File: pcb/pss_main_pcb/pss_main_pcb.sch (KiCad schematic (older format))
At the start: 29 parts

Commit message: Fix schematics
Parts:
- removed C?: C, symbol Device:C
- removed R?: R, symbol Device:R
- added R?: 1k, symbol Device:R
- C? (x2): value 680uF/50V -> 470uF/50V
- C?: value 220uF/16V -> 270uF/10V
- C?: value 220uF/16V -> 330uF/10V
- L?: value 33uH -> 68uH
- L?: value 33uH -> 47uH
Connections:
- net +3V3: now also R?.1
- net GND: no longer U?.5 (~ON~/OFF)
- new net Enable_5V: R?.2, U?.5 (~ON~/OFF)
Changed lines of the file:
@@
 Wire Wire Line
 	9950 1500 9950 1650
-$Comp
-L Device:R R?
-U 1 1 5E946DFD
-P 10350 1700
-F 0 "R?" H 10420 1746 50  0000 L CNN
-F 1 "R" H 10420 1655 50  0000 L CNN
-F 2 "" V 10280 1700 50  0001 C CNN
-F 3 "~" H 10350 1700 50  0001 C CNN
-	1    10350 1700
-	1    0    0    -1
-$EndComp
-$Comp
-L Device:C C?
-U 1 1 5E946EC3
-P 10350 2050
-F 0 "C?" H 10465 2096 50  0000 L CNN
-F 1 "C" H 10465 2005 50  0000 L CNN
-F 2 "" H 10388 1900 50  0001 C CNN
-F 3 "~" H 10350 2050 50  0001 C CNN
-	1    10350 2050
-	1    0    0    -1
-$EndComp
 Wire Notes Line
 	600  700  2450 700
@@
 P 3550 1400
 F 0 "C?" H 3300 1450 50  0000 L CNN
-F 1 "680uF/50V" H 2950 1350 50  0000 L CNN
+F 1 "470uF/50V" H 2950 1350 50  0000 L CNN
 F 2 "" H 3550 1400 50  0001 C CNN
 F 3 "~" H 3550 1400 50  0001 C CNN
@@
 	3550 1150 3900 1150
 Connection ~ 3550 1150
-Wire Wire Line
-	3900 1350 3900 1600
-Wire Wire Line
-	3900 1600 3550 1600
 Connection ~ 3550 1600
 Wire Wire Line
 	4400 1550 4400 1600
-Wire Wire Line
-	4400 1600 3900 1600
-Connection ~ 3900 1600
 $Comp
 L Device:L L?
@@
 P 5550 1350
 F 0 "L?" V 5500 1350 50  0000 C CNN
-F 1 "33uH" V 5650 1350 50  0000 C CNN
+F 1 "68uH" V 5650 1350 50  0000 C CNN
 F 2 "" H 5550 1350 50  0001 C CNN
 F 3 "~" H 5550 1350 50  0001 C CNN
@@
 P 6100 1600
 F 0 "C?" H 6215 1646 50  0000 L CNN
-F 1 "220uF/16V" H 6215 1555 50  0000 L CNN
+F 1 "270uF/10V" H 6215 1555 50  0000 L CNN
 F 2 "" H 6100 1600 50  0001 C CNN
 F 3 "~" H 6100 1600 50  0001 C CNN
@@
 P 4350 2700
 F 0 "C?" H 4100 2750 50  0000 L CNN
-F 1 "680uF/50V" H 3750 2650 50  0000 L CNN
+F 1 "470uF/50V" H 3750 2650 50  0000 L CNN
 F 2 "" H 4350 2700 50  0001 C CNN
 F 3 "~" H 4350 2700 50  0001 C CNN
@@
 P 6350 2650
 F 0 "L?" V 6300 2650 50  0000 C CNN
-F 1 "33uH" V 6450 2650 50  0000 C CNN
+F 1 "47uH" V 6450 2650 50  0000 C CNN
 F 2 "" H 6350 2650 50  0001 C CNN
 F 3 "~" H 6350 2650 50  0001 C CNN
@@
 P 6900 2900
 F 0 "C?" H 7015 2946 50  0000 L CNN
-F 1 "220uF/16V" H 7015 2855 50  0000 L CNN
+F 1 "330uF/10V" H 7015 2855 50  0000 L CNN
 F 2 "" H 6900 2900 50  0001 C CNN
 F 3 "~" H 6900 2900 50  0001 C CNN
@@
 Wire Wire Line
 	9950 1100 10550 1100
-Wire Wire Line
-	9950 1500 10350 1500
-Wire Wire Line
-	10350 1550 10350 1500
-Connection ~ 10350 1500
-Wire Wire Line
-	10350 1500 10550 1500
-Wire Wire Line
-	10350 1900 10350 1850
 $Comp
 L Transistors_custom:MMBT2222 Q?
@@
 	9950 2050 9950 2400
 Wire Wire Line
-	9950 2400 10350 2400
-Wire Wire Line
-	10350 2200 10350 2400
-Wire Wire Line
 	8300 2100 8200 2100
 Wire Wire Line
@@
 Text Notes 8300 850  0    50   ~ 0
 Soldering Iron Heat Controls\n
+Wire Wire Line
+	3550 1600 4400 1600
+$Comp
+L power:+3.3V #PWR?
+U 1 1 5E92E41F
+P 4200 1850
+F 0 "#PWR?" H 4200 1700 50  0001 C CNN
+F 1 "+3.3V" H 4215 2023 50  0000 C CNN
+F 2 "" H 4200 1850 50  0001 C CNN
+F 3 "" H 4200 1850 50  0001 C CNN
+	1    4200 1850
+	1    0    0    -1
+$EndComp
+Text GLabel 3450 1850 0    50   Input ~ 0
+Enable_5V
+$Comp
+L Device:R R?
+U 1 1 5E92E514
+P 3950 1850
+F 0 "R?" V 3743 1850 50  0000 C CNN
+F 1 "1k" V 3834 1850 50  0000 C CNN
+F 2 "" V 3880 1850 50  0001 C CNN
+F 3 "~" H 3950 1850 50  0001 C CNN
+	1    3950 1850
+	0    1    1    0
+$EndComp
+Wire Wire Line
+	4100 1850 4200 1850
+Wire Wire Line
+	3900 1350 3750 1350
+Wire Wire Line
+	3750 1350 3750 1850
+Wire Wire Line
+	3750 1850 3800 1850
+Wire Wire Line
+	3750 1850 3450 1850
+Connection ~ 3750 1850
+Wire Wire Line
+	9950 1500 10550 1500
 $EndSCHEMATC

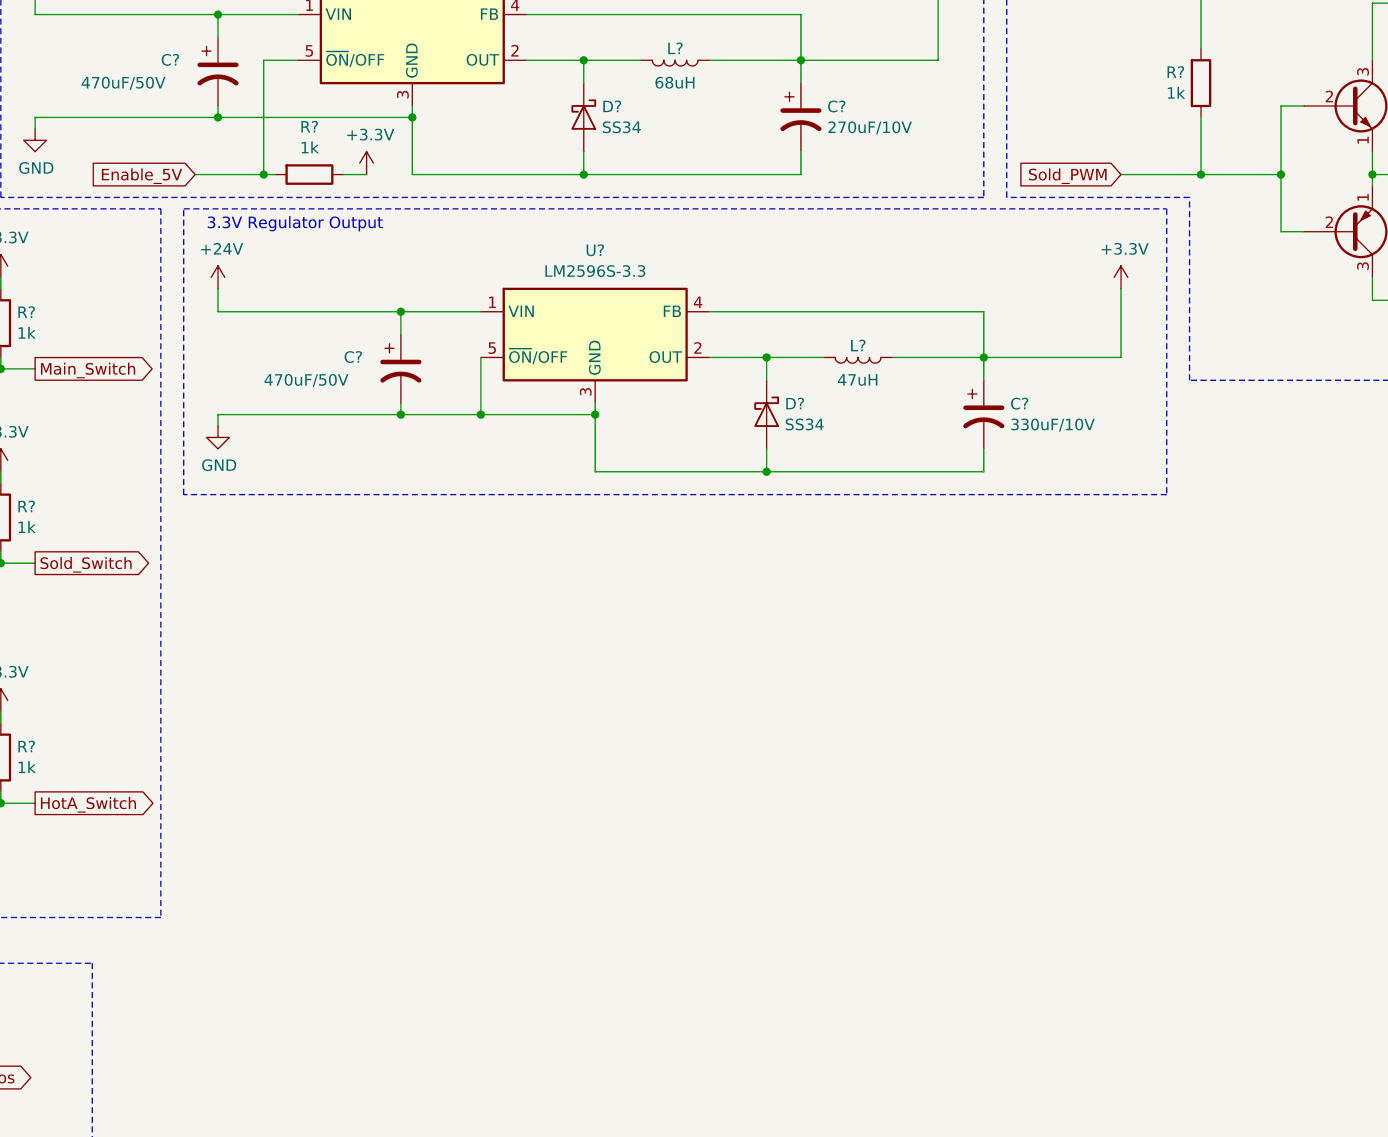
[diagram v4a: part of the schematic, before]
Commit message: Add 220v controls schematics
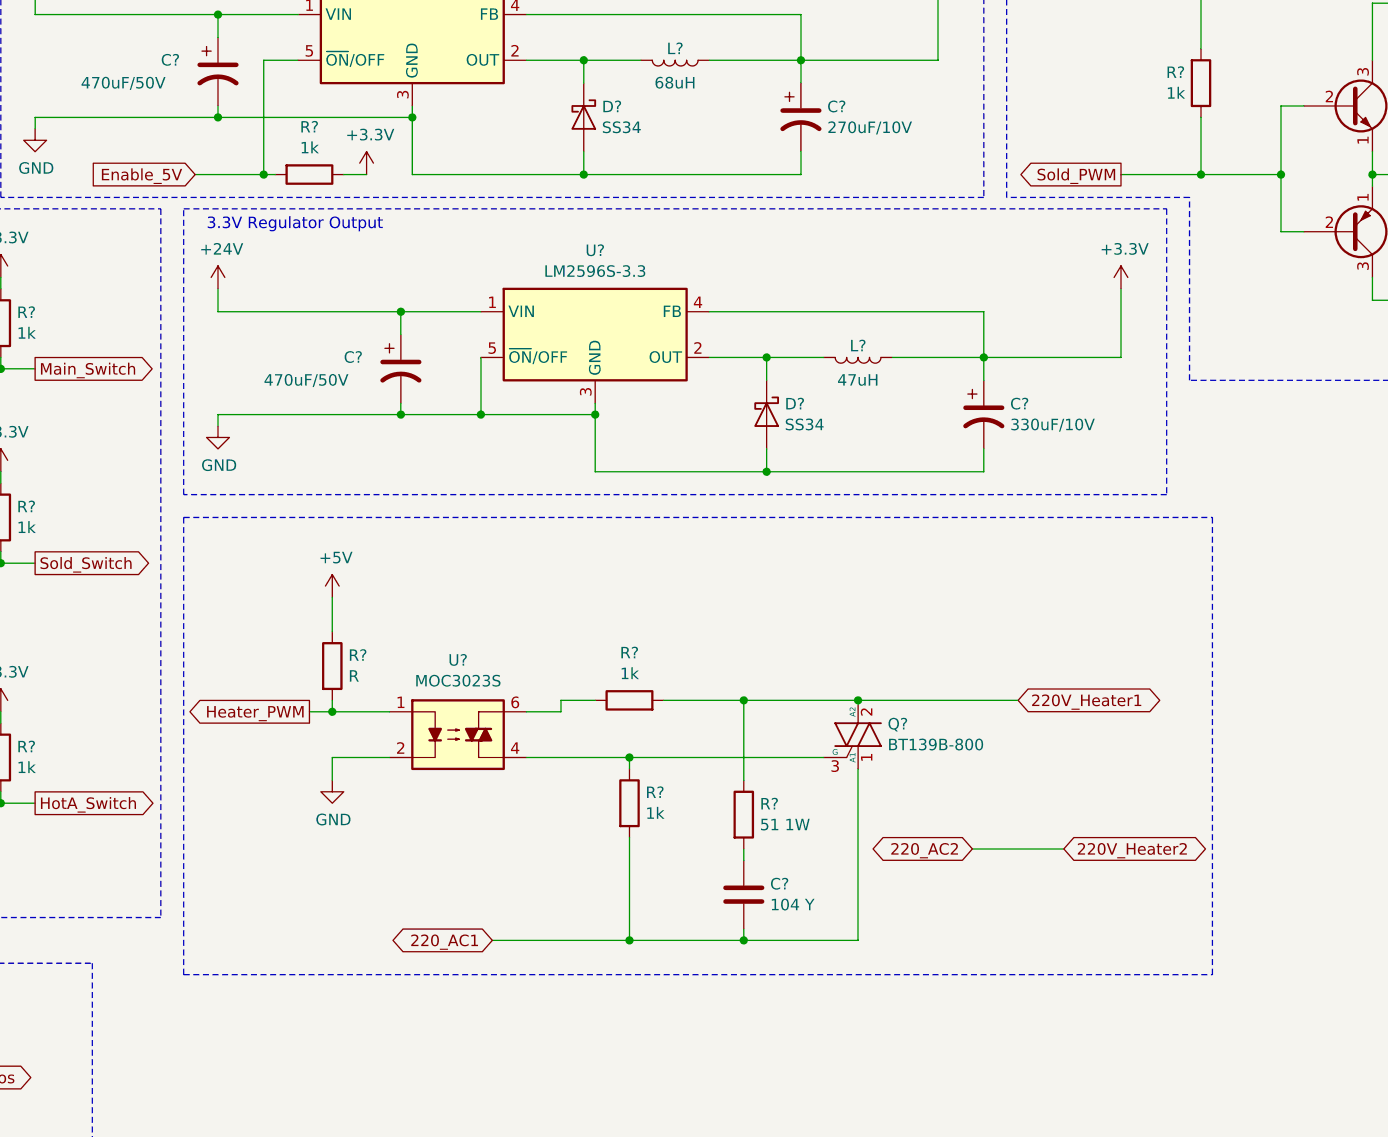
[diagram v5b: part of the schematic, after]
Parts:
- added C?: 104 Y, symbol Device:C
- added Q?: BT139B-800, Package_TO_SOT_THT:SOT-404, symbol Triac_custom:BT139B-800
- added R?: R, symbol Device:R
- added R? (x2): 1k, symbol Device:R
- added R?: 51 1W, symbol Device:R
- added U?: MOC3023S, symbol Opto_custom:MOC3023S
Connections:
- net 220_AC2 is gone; now on net 220V_Heater2: J?.1 (Pin_1)
- net +5V: now also R?.1
- net 220V_Heater1: now also Q?.2 (A2), R?.1, R?.2
- net 220_AC1: now also C?.2, Q?.1 (A1), R?.2
- net GND: now also U?.2
- new net: Q?.3 (G), R?.1, U?.4
- new net: R?.1, U?.6
- new net: C?.1, R?.2
- new net Heater_PWM: R?.2, U?.1
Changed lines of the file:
@@
 Text Notes 650  2100 0    50   ~ 0
 Encoders Inputs
-Text GLabel 7500 1850 0    50   Input ~ 0
+Text GLabel 7500 1850 0    50   Output ~ 0
 Sold_PWM
 $Comp
@@
 Wire Wire Line
 	9950 1500 10550 1500
+$Comp
+L power:+5V #PWR?
+U 1 1 5E941771
+P 4050 3700
+F 0 "#PWR?" H 4050 3550 50  0001 C CNN
+F 1 "+5V" H 4065 3873 50  0000 C CNN
+F 2 "" H 4050 3700 50  0001 C CNN
+F 3 "" H 4050 3700 50  0001 C CNN
+	1    4050 3700
+	1    0    0    -1
+$EndComp
+$Comp
+L Device:R R?
+U 1 1 5E941873
+P 4050 4000
+F 0 "R?" H 4120 4046 50  0000 L CNN
+F 1 "R" H 4120 3955 50  0000 L CNN
+F 2 "" V 3980 4000 50  0001 C CNN
+F 3 "~" H 4050 4000 50  0001 C CNN
+	1    4050 4000
+	1    0    0    -1
+$EndComp
+$Comp
+L Opto_custom:MOC3023S U?
+U 1 1 5E941A1A
+P 4600 4300
+F 0 "U?" H 4600 4625 50  0000 C CNN
+F 1 "MOC3023S" H 4600 4534 50  0000 C CNN
+F 2 "" H 4400 4100 50  0001 L CIN
+F 3 "https://optoelectronics.liteon.com/upload/download/DS-70-99-0019/MOC302X%20series%20201606.pdf" H 4575 4300 50  0001 L CNN
+	1    4600 4300
+	1    0    0    -1
+$EndComp
+$Comp
+L Triac_custom:BT139B-800 Q?
+U 1 1 5E9467AF
+P 6350 4300
+F 0 "Q?" H 6479 4346 50  0000 L CNN
+F 1 "BT139B-800" H 6479 4255 50  0000 L CNN
+F 2 "Package_TO_SOT_THT:SOT-404" H 6550 4225 50  0001 L CIN
+F 3 "https://www.ariat-tech.com/datasheet/42/SBR545D1-13.pdf" H 6350 4300 50  0001 L CNN
+	1    6350 4300
+	1    0    0    -1
+$EndComp
+$Comp
+L power:GND #PWR?
+U 1 1 5E946913
+P 4050 4500
+F 0 "#PWR?" H 4050 4250 50  0001 C CNN
+F 1 "GND" H 4055 4327 50  0000 C CNN
+F 2 "" H 4050 4500 50  0001 C CNN
+F 3 "" H 4050 4500 50  0001 C CNN
+	1    4050 4500
+	1    0    0    -1
+$EndComp
+Text GLabel 4750 5200 0    50   BiDi ~ 0
+220_AC1
+Text GLabel 6850 4800 0    50   BiDi ~ 0
+220_AC2
+$Comp
+L Device:R R?
+U 1 1 5E94AD12
+P 5350 4600
+F 0 "R?" H 5420 4646 50  0000 L CNN
+F 1 "1k" H 5420 4555 50  0000 L CNN
+F 2 "" V 5280 4600 50  0001 C CNN
+F 3 "~" H 5350 4600 50  0001 C CNN
+	1    5350 4600
+	1    0    0    -1
+$EndComp
+$Comp
+L Device:R R?
+U 1 1 5E94B248
+P 5850 4650
+F 0 "R?" H 5920 4696 50  0000 L CNN
+F 1 "51 1W" H 5920 4605 50  0000 L CNN
+F 2 "" V 5780 4650 50  0001 C CNN
+F 3 "~" H 5850 4650 50  0001 C CNN
+	1    5850 4650
+	1    0    0    -1
+$EndComp
+$Comp
+L Device:R R?
+U 1 1 5E94B2DF
+P 5350 4150
+F 0 "R?" V 5557 4150 50  0000 C CNN
+F 1 "1k" V 5466 4150 50  0000 C CNN
+F 2 "" V 5280 4150 50  0001 C CNN
+F 3 "~" H 5350 4150 50  0001 C CNN
+	1    5350 4150
+	0    -1   -1   0
+$EndComp
+$Comp
+L Device:C C?
+U 1 1 5E94B396
+P 5850 5000
+F 0 "C?" H 5965 5046 50  0000 L CNN
+F 1 "104 Y" H 5965 4955 50  0000 L CNN
+F 2 "" H 5888 4850 50  0001 C CNN
+F 3 "~" H 5850 5000 50  0001 C CNN
+	1    5850 5000
+	1    0    0    -1
+$EndComp
+Text GLabel 7050 4150 2    50   BiDi ~ 0
+220V_Heater1
+Text GLabel 7250 4800 2    50   BiDi ~ 0
+220V_Heater2
+Wire Wire Line
+	4900 4400 5350 4400
+Wire Wire Line
+	4900 4200 5050 4200
+Wire Wire Line
+	5050 4200 5050 4150
+Wire Wire Line
+	5050 4150 5200 4150
+Wire Wire Line
+	5500 4150 5850 4150
+Wire Wire Line
+	5350 4450 5350 4400
+Connection ~ 5350 4400
+Wire Wire Line
+	5350 4400 6200 4400
+Wire Wire Line
+	4750 5200 5350 5200
+Wire Wire Line
+	5350 5200 5850 5200
+Connection ~ 5350 5200
+Wire Wire Line
+	5850 5200 5850 5150
+Connection ~ 5850 5200
+Wire Wire Line
+	5850 5200 6350 5200
+Wire Wire Line
+	5350 4750 5350 5200
+Wire Wire Line
+	5850 4850 5850 4800
+Wire Wire Line
+	5850 4500 5850 4150
+Connection ~ 5850 4150
+Wire Wire Line
+	5850 4150 6350 4150
+Wire Wire Line
+	6350 4450 6350 5200
+Wire Wire Line
+	6350 4150 7050 4150
+Connection ~ 6350 4150
+Wire Wire Line
+	4050 3850 4050 3700
+Wire Wire Line
+	4300 4200 4050 4200
+Wire Wire Line
+	4050 4200 4050 4150
+Wire Wire Line
+	4050 4500 4050 4400
+Wire Wire Line
+	4050 4400 4300 4400
+Text GLabel 3950 4200 0    50   Output ~ 0
+Heater_PWM
+Wire Wire Line
+	4050 4200 3950 4200
+Connection ~ 4050 4200
+Wire Wire Line
+	6850 4800 7250 4800
+Wire Notes Line
+	3400 3350 7900 3350
+Wire Notes Line
+	7900 3350 7900 5350
+Wire Notes Line
+	3400 5350 7900 5350
+Wire Notes Line
+	3400 3350 3400 5350
 $EndSCHEMATC

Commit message: Add small changes to schematics
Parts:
- R?: value R -> 1k
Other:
- note added: "Hot Air Gun Heater Controls\n"
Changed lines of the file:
@@
 P 4050 4000
 F 0 "R?" H 4120 4046 50  0000 L CNN
-F 1 "R" H 4120 3955 50  0000 L CNN
+F 1 "1k" H 4120 3955 50  0000 L CNN
 F 2 "" V 3980 4000 50  0001 C CNN
 F 3 "~" H 4050 4000 50  0001 C CNN
@@
 Wire Notes Line
 	3400 3350 3400 5350
+Text Notes 4800 3450 0    50   ~ 0
+Hot Air Gun Heater Controls\n
 $EndSCHEMATC

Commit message: Add fan controls schematics
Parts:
- added C?: 47uF 50V, symbol Device:CP1
- added C?: 1uF 50V, symbol Device:CP1
- added D?: D, symbol Device:D
- added L?: 1uH, symbol Device:L
- added Q?: IRLML9301T, Package_TO_SOT_SMD:SOT-23, symbol Transistors_custom:IRLML9301T
- added Q?: BC817, Package_TO_SOT_SMD:SOT-23, symbol Transistor_BJT:BC817
- added R?: 10k, symbol Device:R
- added R?: 1k, symbol Device:R
- added R?: 1K, symbol Device:R
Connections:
- net +24V: now also Q?.2 (S), R?.1
- net +5V: now also R?.2
- net GND: now also C?.2, C?.2, D?.2 (A), Q?.2 (E)
- net Hot_Air_Fan: now also C?.1, D?.1 (K), L?.2
- new net: Q?.1 (G), R?.1
- new net: C?.1, L?.1, Q?.3 (D)
- new net: Q?.3 (C), R?.2, R?.2
- new net Fan_PWM: Q?.1 (B), R?.1
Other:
- note added: "Hot Air Gun Fun Controls\n"
